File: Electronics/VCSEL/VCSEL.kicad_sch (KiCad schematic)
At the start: 10 parts, among them J1 Conn_01x06

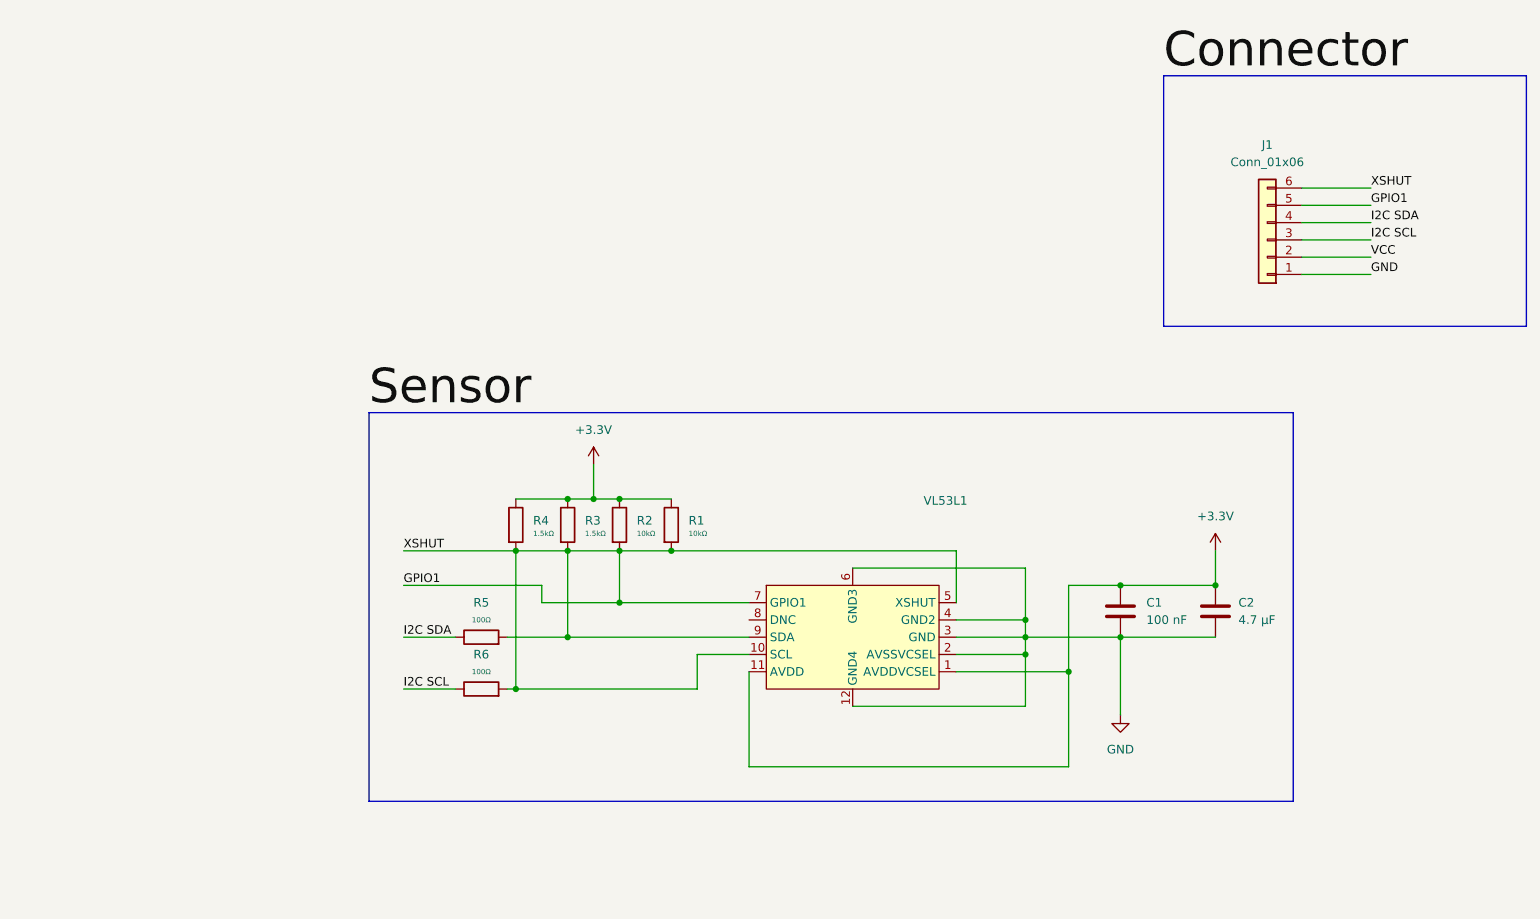
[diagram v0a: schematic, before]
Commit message: project setup for VCSEL
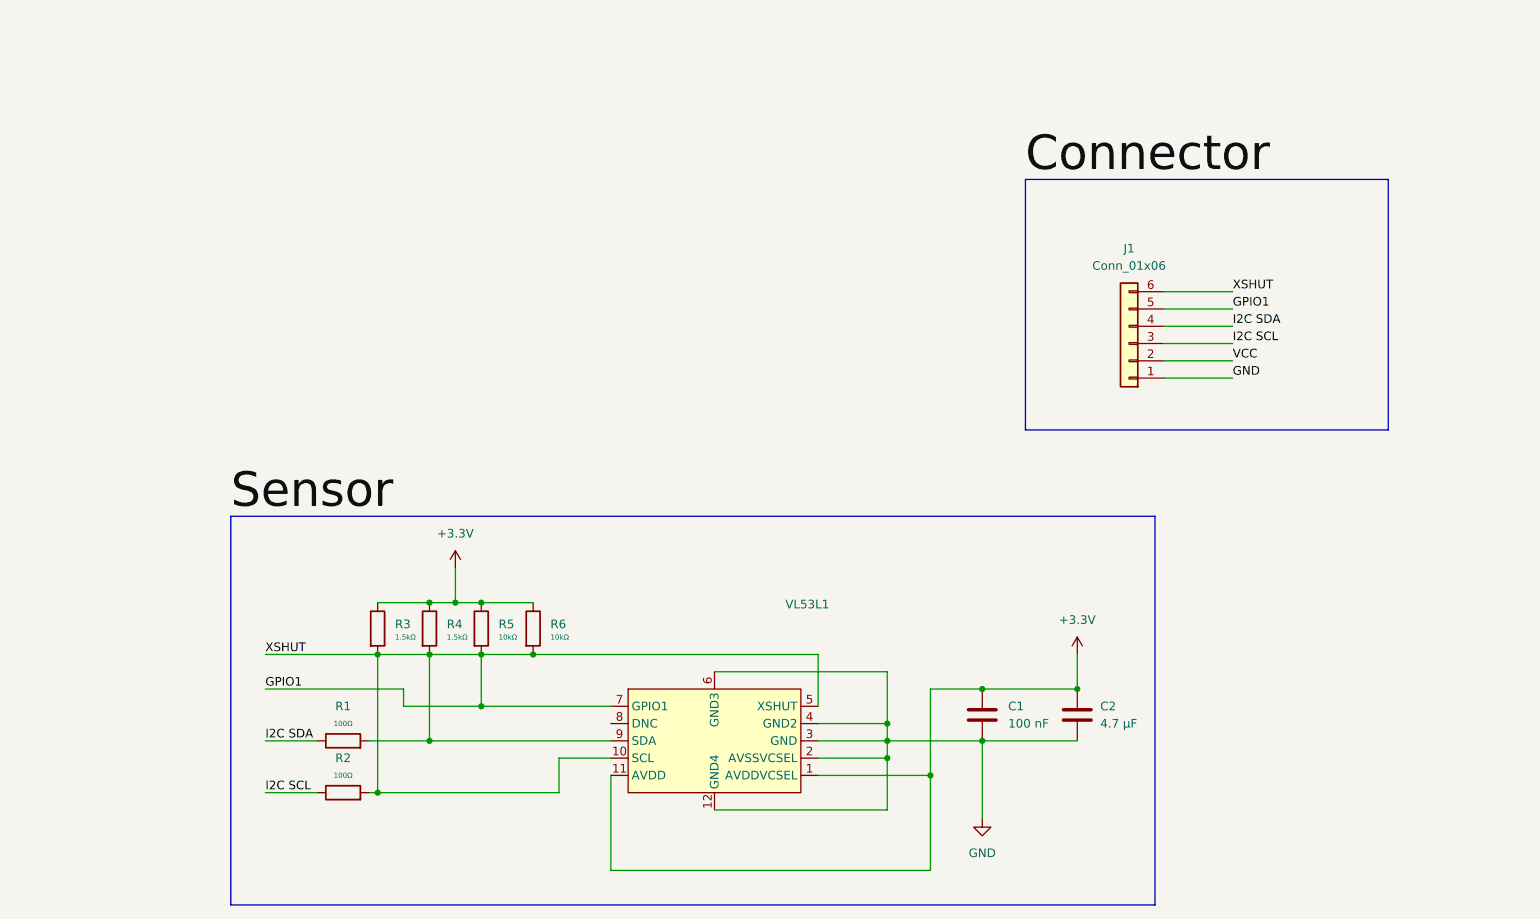
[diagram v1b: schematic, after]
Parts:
- R1, R2: value 10kΩ -> 100Ω
- R5, R6: value 100Ω -> 10kΩ
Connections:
- net +3.3V: now also R5.1, R6.1; no longer R1.1, R2.1
- net I2C SCL: now also R2.1; no longer R6.1
- net I2C SDA: now also R1.1; no longer R5.1

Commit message: V01 VCSEL PCB added
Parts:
- removed J1: Conn_01x06, symbol Connector_Generic:Conn_01x06
- added J2: Conn_01x04, Connector_JST:JST_EH_B4B-EH-A_1x04_P2.50mm_Vertical, symbol Connector_Generic:Conn_01x04
- added U1: TPS82698SIPR, footprints:SIP0008A, symbol 2024-11-04_05-34-17:TPS82698SIPR
- C1, C2: footprint (none) -> Capacitor_SMD:C_0402_1005Metric
- R1, R2, R5, R6: footprint (none) -> Resistor_SMD:R_0402_1005Metric
- R3, R4: footprint (none) -> Resistor_SMD:R_01005_0402Metric
- VL53L1: footprint (none) -> VCSEL_footprints:QFN_BV0FY&slash_1_STM
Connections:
- net GND: now also U1.B1 (MODE), U1.C1 (GND), U1.C2 (GND), U1.C3 (GND)
- net GPIO1: now also J2.3 (Pin_3), J2.4 (Pin_4)
- net I2C SCL: now also J2.1 (Pin_1)
- net I2C SDA: now also J2.2 (Pin_2)
- net +3.3V: no longer names the net of C1.1, C2.1, R3.1, R4.1, R5.1, R6.1, VL53L1.1 (AVDDVCSEL), VL53L1.11 (AVDD)
- net +3.3V: now also U1.A1 (VOUT)
- new net +5V: U1.A2 (VIN), U1.A3 (VIN), U1.B2 (EN)
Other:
- company: (none) -> Georgia Tech Propulsive Landers
- title: (none) -> VCSEL - VL53L1
- moved on the sheet: C1, C2, R1, R2, R3, R4, R5, R6, VL53L1
